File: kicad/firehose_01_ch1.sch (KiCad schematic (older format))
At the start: 82 parts, among them J1 SMA, U1 MAX2112, U2 MAX19505, U20 MIC2090-1YM5, U3 MGA-68563

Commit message: more KiCAD schematic
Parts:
- C31, C32, C33, C34, C35, C36: renamed from C?; value C -> 0.1 uF
- FB11, FB14: value FB -> 240
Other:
- moved on the sheet: C21, C22, C23, C24, C25, C26, C31, C32, C33, C34, C35, C36

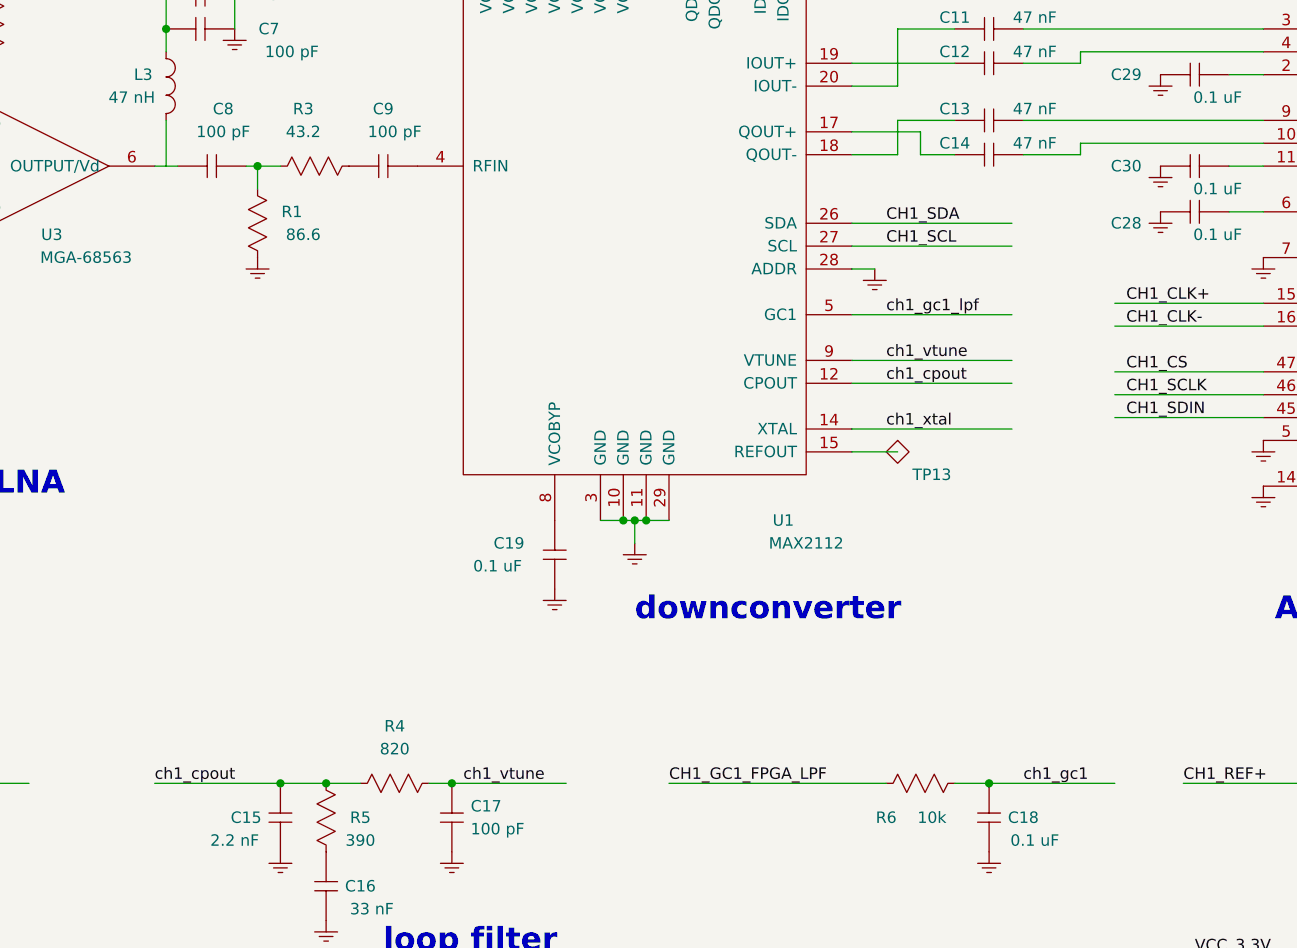
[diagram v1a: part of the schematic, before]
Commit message: fix KiCAD power symbol
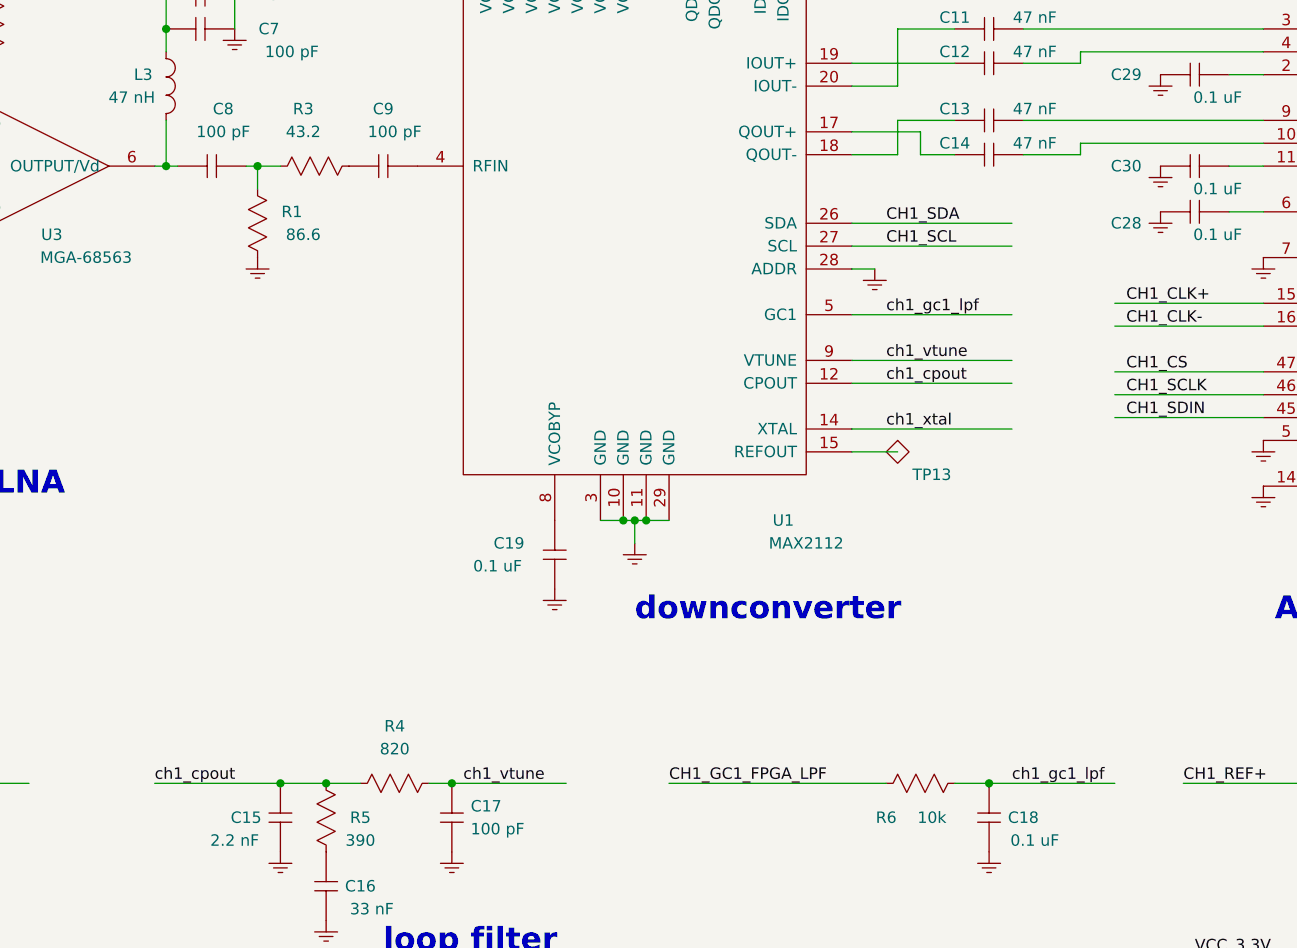
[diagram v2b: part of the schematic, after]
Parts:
- removed PWR? (x25): GND, symbol GND
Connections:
- net labels added: GND
- net labels removed: ch1_gc1
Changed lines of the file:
@@
 EESchema Schematic File Version 2
 LIBS:GNSS_Firehose
-LIBS:device
 LIBS:GNSS_Firehose-cache
 EELAYER 25 0
@@
 $EndComp
 $Comp
-L GND PWR?
+L GND #PWR03
 U 1 1 58CCB8E4
 P 1400 3500
-F 0 "PWR?" H 1600 3400 50  0001 C CNN
+F 0 "#PWR03" H 1600 3400 50  0001 C CNN
 F 1 "GND" H 1600 3300 50  0001 C CNN
 F 2 "" H 1400 3500 50  0001 C CNN
@@
 $EndComp
 $Comp
-L GND PWR?
+L GND #PWR04
 U 1 1 58CCBA24
 P 700 3300
-F 0 "PWR?" H 900 3200 50  0001 C CNN
+F 0 "#PWR04" H 900 3200 50  0001 C CNN
 F 1 "GND" H 900 3100 50  0001 C CNN
 F 2 "" H 700 3300 50  0001 C CNN
@@
 $EndComp
 $Comp
-L GND PWR?
+L GND #PWR05
 U 1 1 58CCC43E
 P 1900 2000
-F 0 "PWR?" H 2100 1900 50  0001 C CNN
+F 0 "#PWR05" H 2100 1900 50  0001 C CNN
 F 1 "GND" H 2100 1800 50  0001 C CNN
 F 2 "" H 1900 2000 50  0001 C CNN
@@
 $EndComp
 $Comp
-L GND PWR?
+L GND #PWR06
 U 1 1 58CCC479
 P 2200 3650
-F 0 "PWR?" H 2400 3550 50  0001 C CNN
+F 0 "#PWR06" H 2400 3550 50  0001 C CNN
 F 1 "GND" H 2400 3450 50  0001 C CNN
 F 2 "" H 2200 3650 50  0001 C CNN
@@
 $EndComp
 $Comp
-L GND PWR?
+L GND #PWR07
 U 1 1 58CCC4B4
 P 3450 3500
-F 0 "PWR?" H 3650 3400 50  0001 C CNN
+F 0 "#PWR07" H 3650 3400 50  0001 C CNN
 F 1 "GND" H 3650 3300 50  0001 C CNN
 F 2 "" H 3450 3500 50  0001 C CNN
@@
 $EndComp
 $Comp
-L GND PWR?
+L GND #PWR08
 U 1 1 58CCC4EF
 P 5100 4750
-F 0 "PWR?" H 5300 4650 50  0001 C CNN
+F 0 "#PWR08" H 5300 4650 50  0001 C CNN
 F 1 "GND" H 5300 4550 50  0001 C CNN
 F 2 "" H 5100 4750 50  0001 C CNN
@@
 $EndComp
 $Comp
-L GND PWR?
+L GND #PWR09
 U 1 1 58CCC5A0
 P 8700 5050
-F 0 "PWR?" H 8900 4950 50  0001 C CNN
+F 0 "#PWR09" H 8900 4950 50  0001 C CNN
 F 1 "GND" H 8900 4850 50  0001 C CNN
 F 2 "" H 8700 5050 50  0001 C CNN
@@
 $EndComp
 $Comp
-L GND PWR?
+L GND #PWR010
 U 1 1 58CCD64A
 P 3350 2500
-F 0 "PWR?" H 3550 2400 50  0001 C CNN
+F 0 "#PWR010" H 3550 2400 50  0001 C CNN
 F 1 "GND" H 3550 2300 50  0001 C CNN
 F 2 "" H 3350 2500 50  0001 C CNN
@@
 $EndComp
 $Comp
-L GND PWR?
+L GND #PWR011
 U 1 1 58CCEBB6
 P 6150 3550
-F 0 "PWR?" H 6350 3450 50  0001 C CNN
+F 0 "#PWR011" H 6350 3450 50  0001 C CNN
 F 1 "GND" H 6350 3350 50  0001 C CNN
 F 2 "" H 6150 3550 50  0001 C CNN
@@
 $EndComp
 $Comp
-L GND PWR?
+L GND #PWR012
 U 1 1 58CCEC6F
 P 4750 4950
-F 0 "PWR?" H 4950 4850 50  0001 C CNN
+F 0 "#PWR012" H 4950 4850 50  0001 C CNN
 F 1 "GND" H 4950 4750 50  0001 C CNN
 F 2 "" H 4750 4950 50  0001 C CNN
@@
 $EndComp
 $Comp
-L GND PWR?
+L GND #PWR013
 U 1 1 58CCF4F3
 P 7400 3300
-F 0 "PWR?" H 7600 3200 50  0001 C CNN
+F 0 "#PWR013" H 7600 3200 50  0001 C CNN
 F 1 "GND" H 7600 3100 50  0001 C CNN
 F 2 "" H 7400 3300 50  0001 C CNN
@@
 $EndComp
 $Comp
-L GND PWR?
+L GND #PWR014
 U 1 1 58CCF5B6
 P 7400 3100
-F 0 "PWR?" H 7600 3000 50  0001 C CNN
+F 0 "#PWR014" H 7600 3000 50  0001 C CNN
 F 1 "GND" H 7600 2900 50  0001 C CNN
 F 2 "" H 7400 3100 50  0001 C CNN
@@
 $EndComp
 $Comp
-L GND PWR?
+L GND #PWR015
 U 1 1 58CCF618
 P 7400 2700
-F 0 "PWR?" H 7600 2600 50  0001 C CNN
+F 0 "#PWR015" H 7600 2600 50  0001 C CNN
 F 1 "GND" H 7600 2500 50  0001 C CNN
 F 2 "" H 7400 2700 50  0001 C CNN
@@
 $EndComp
 $Comp
-L GND PWR?
+L GND #PWR016
 U 1 1 58CD033B
 P 7850 3500
-F 0 "PWR?" H 8050 3400 50  0001 C CNN
+F 0 "#PWR016" H 8050 3400 50  0001 C CNN
 F 1 "GND" H 8050 3300 50  0001 C CNN
 F 2 "" H 7850 3500 50  0001 C CNN
@@
 $EndComp
 $Comp
-L GND PWR?
+L GND #PWR017
 U 1 1 58CD0FE4
 P 7850 4300
-F 0 "PWR?" H 8050 4200 50  0001 C CNN
+F 0 "#PWR017" H 8050 4200 50  0001 C CNN
 F 1 "GND" H 8050 4100 50  0001 C CNN
 F 2 "" H 7850 4300 50  0001 C CNN
@@
 $EndComp
 $Comp
-L GND PWR?
+L GND #PWR018
 U 1 1 58CD1046
 P 7850 4500
-F 0 "PWR?" H 8050 4400 50  0001 C CNN
+F 0 "#PWR018" H 8050 4400 50  0001 C CNN
 F 1 "GND" H 8050 4300 50  0001 C CNN
 F 2 "" H 7850 4500 50  0001 C CNN
@@
 $EndComp
 $Comp
-L GND PWR?
+L GND #PWR019
 U 1 1 58CD3173
 P 2000 6100
-F 0 "PWR?" H 2200 6000 50  0001 C CNN
+F 0 "#PWR019" H 2200 6000 50  0001 C CNN
 F 1 "GND" H 2200 5900 50  0001 C CNN
 F 2 "" H 2000 6100 50  0001 C CNN
@@
 $EndComp
 $Comp
-L GND PWR?
+L GND #PWR020
 U 1 1 58CD31ED
 P 3750 6400
-F 0 "PWR?" H 3950 6300 50  0001 C CNN
+F 0 "#PWR020" H 3950 6300 50  0001 C CNN
 F 1 "GND" H 3950 6200 50  0001 C CNN
 F 2 "" H 3750 6400 50  0001 C CNN
@@
 $EndComp
 $Comp
-L GND PWR?
+L GND #PWR021
 U 1 1 58CD3267
 P 4300 6100
-F 0 "PWR?" H 4500 6000 50  0001 C CNN
+F 0 "#PWR021" H 4500 6000 50  0001 C CNN
 F 1 "GND" H 4500 5900 50  0001 C CNN
 F 2 "" H 4300 6100 50  0001 C CNN
@@
 $EndComp
 $Comp
-L GND PWR?
+L GND #PWR022
 U 1 1 58CD32E1
 P 3550 6100
-F 0 "PWR?" H 3750 6000 50  0001 C CNN
+F 0 "#PWR022" H 3750 6000 50  0001 C CNN
 F 1 "GND" H 3750 5900 50  0001 C CNN
 F 2 "" H 3550 6100 50  0001 C CNN
@@
 ch1_vtune
 $Comp
-L GND PWR?
+L GND #PWR023
 U 1 1 58CD60D0
 P 3450 7350
-F 0 "PWR?" H 3650 7250 50  0001 C CNN
+F 0 "#PWR023" H 3650 7250 50  0001 C CNN
 F 1 "GND" H 3650 7150 50  0001 C CNN
 F 2 "" H 3450 7350 50  0001 C CNN
@@
 $EndComp
 $Comp
-L GND PWR?
+L GND #PWR024
 U 1 1 58CD6BF8
 P 8700 6850
-F 0 "PWR?" H 8900 6750 50  0001 C CNN
+F 0 "#PWR024" H 8900 6750 50  0001 C CNN
 F 1 "GND" H 8900 6650 50  0001 C CNN
 F 2 "" H 8700 6850 50  0001 C CNN
@@
 $EndComp
 $Comp
-L GND PWR?
+L GND #PWR025
 U 1 1 58CD6CAE
 P 9900 6850
-F 0 "PWR?" H 10100 6750 50  0001 C CNN
+F 0 "#PWR025" H 10100 6750 50  0001 C CNN
 F 1 "GND" H 10100 6650 50  0001 C CNN
 F 2 "" H 9900 6850 50  0001 C CNN
@@
 	600  1350 1200 1350
 Wire Wire Line
-	3050 2850 3050 3050
-Wire Wire Line
 	3100 3050 3000 3050
 Wire Wire Line
@@
 Text Label 5250 5750 0    50   ~ 0
 CH1_GC1_FPGA_LPF
-Text Label 6800 5750 0    50   ~ 0
-ch1_gc1
+Text Label 6750 5750 0    50   ~ 0
+ch1_gc1_lpf
 Text Label 7500 5750 0    50   ~ 0
 CH1_REF+
@@
 ch1_xtal
 $Comp
-L GND PWR?
+L GND #PWR026
 U 1 1 58CE2E65
 P 6650 6100
-F 0 "PWR?" H 6850 6000 50  0001 C CNN
+F 0 "#PWR026" H 6850 6000 50  0001 C CNN
 F 1 "GND" H 6850 5900 50  0001 C CNN
 F 2 "" H 6650 6100 50  0001 C CNN
@@
 $EndComp
 $Comp
-L GND PWR?
+L GND #PWR027
 U 1 1 58CE2F1B
 P 8050 6100
-F 0 "PWR?" H 8250 6000 50  0001 C CNN
+F 0 "#PWR027" H 8250 6000 50  0001 C CNN
 F 1 "GND" H 8250 5900 50  0001 C CNN
 F 2 "" H 8050 6100 50  0001 C CNN
@@
 Connection ~ 2200 3600
 Connection ~ 3300 7300
+Wire Wire Line
+	3050 2850 3050 3050
+Connection ~ 3050 3050
 $EndSCHEMATC

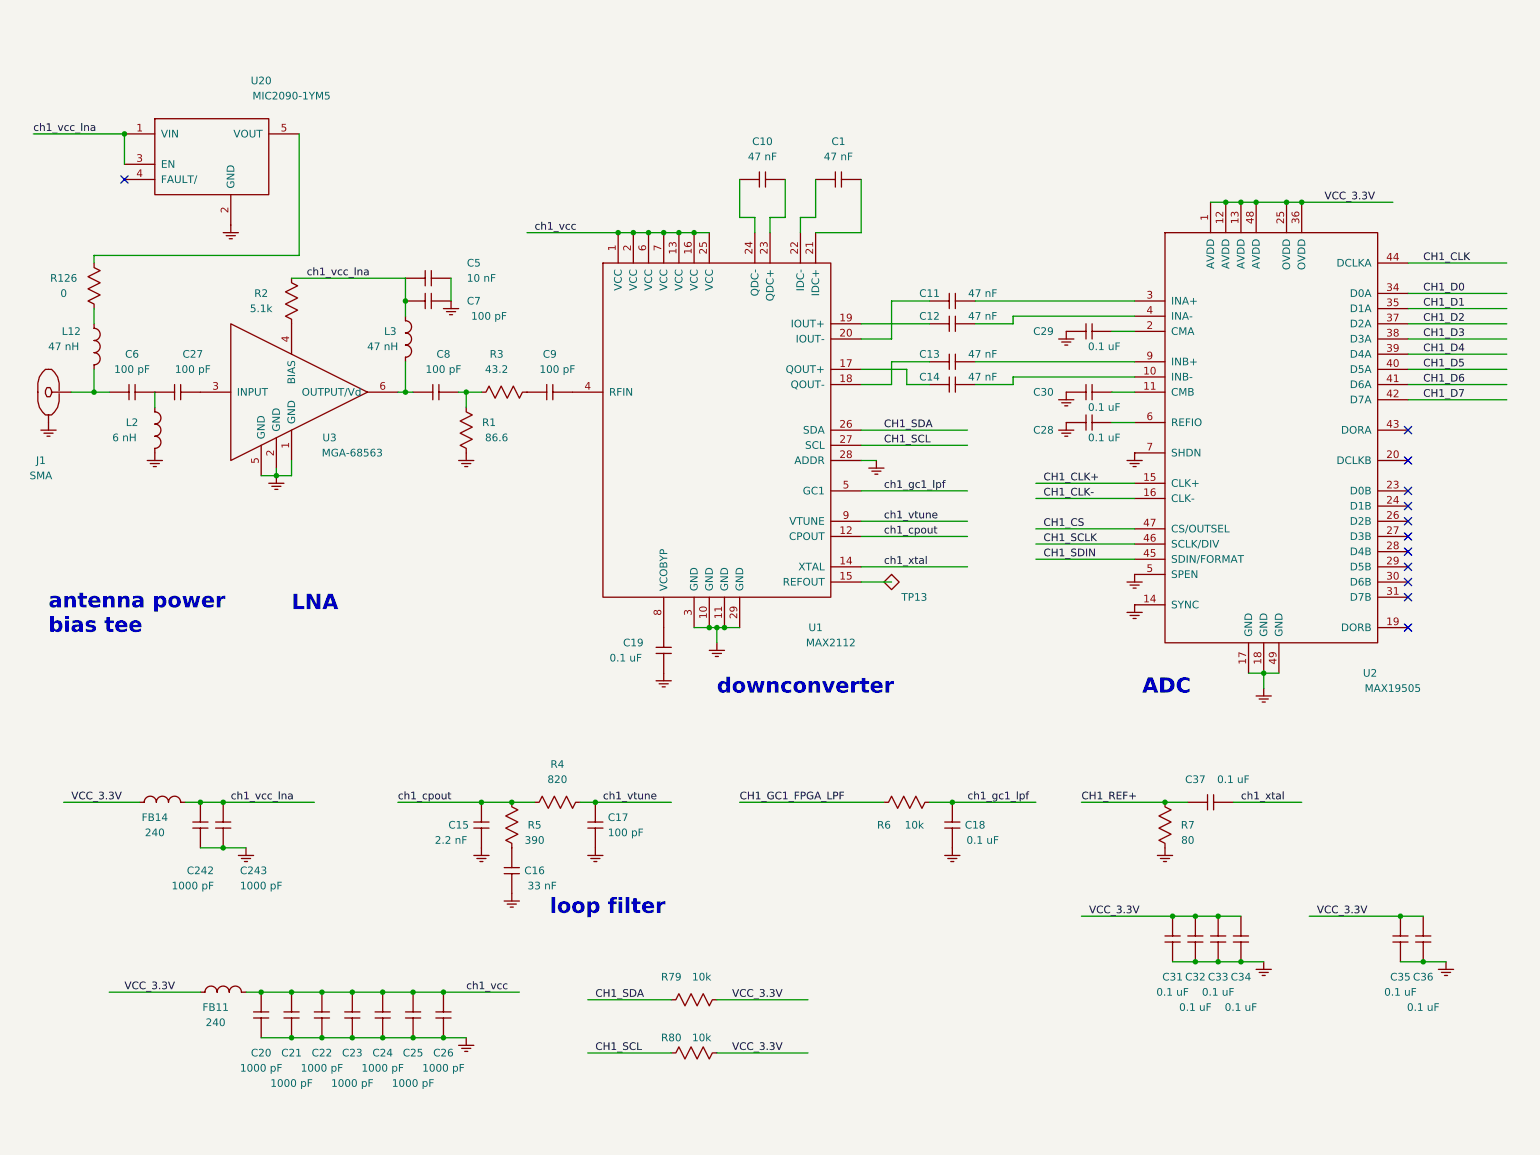
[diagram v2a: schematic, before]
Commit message: schematic, RF channels 2 and 3
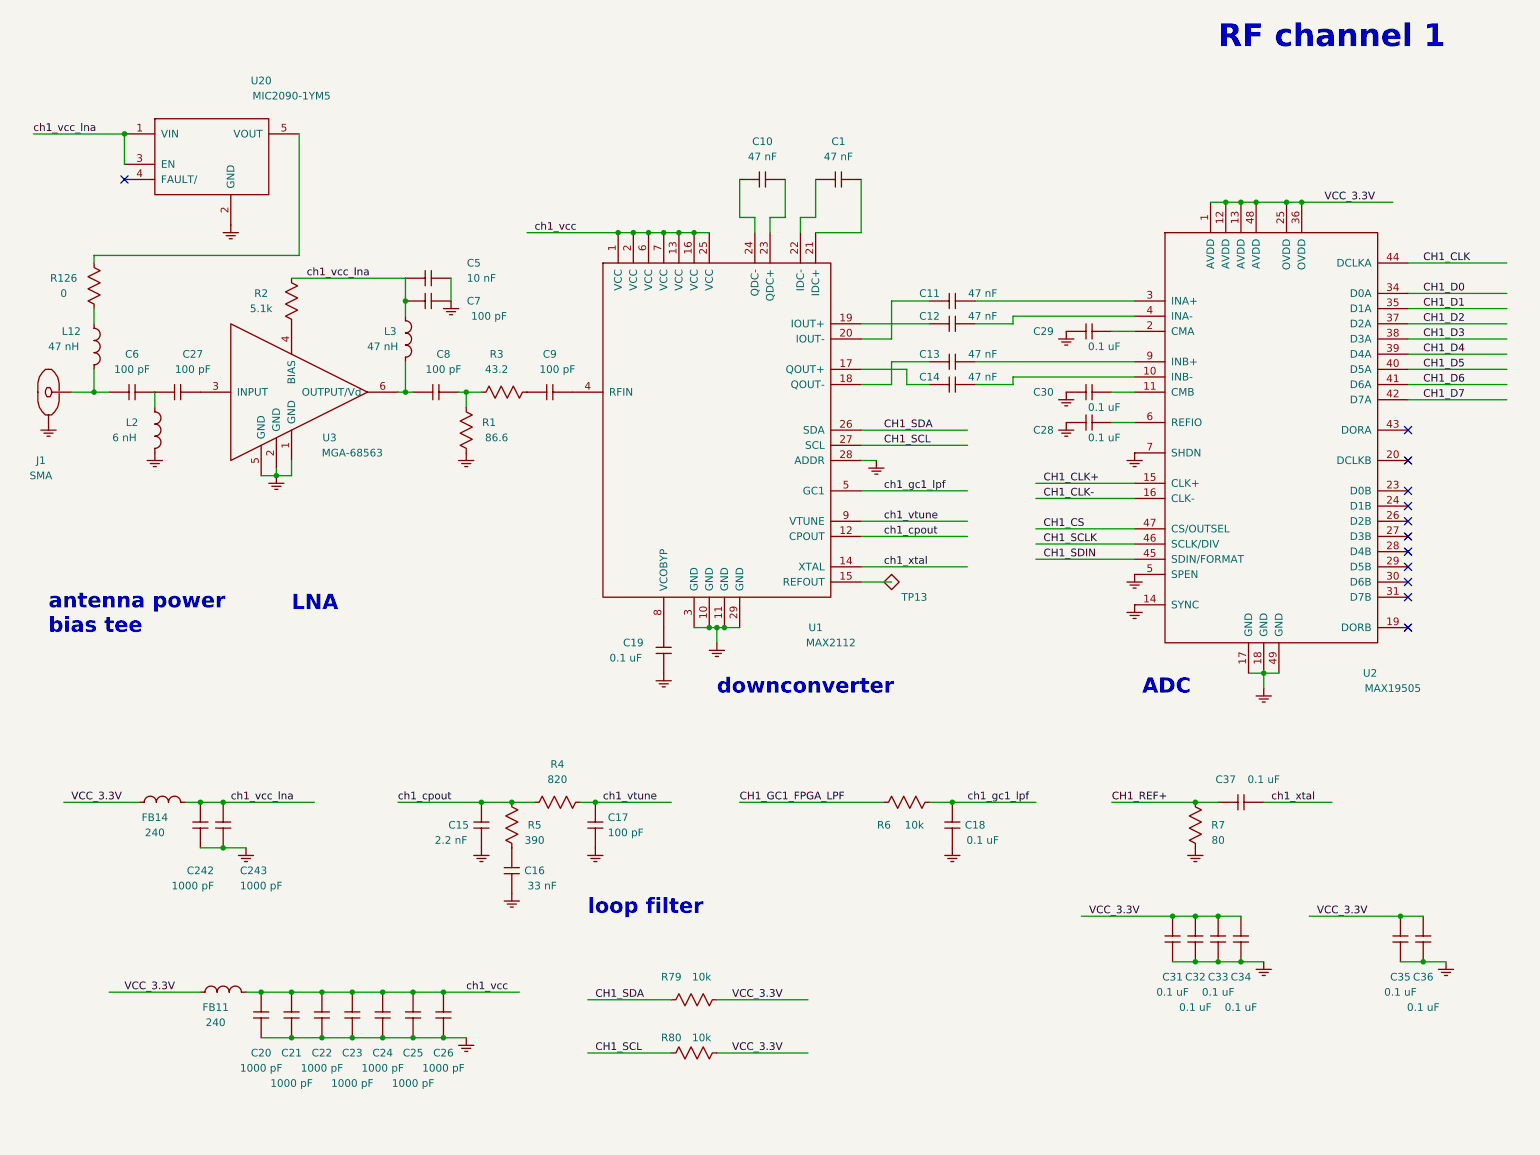
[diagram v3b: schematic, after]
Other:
- note added: "RF channel 1"
- moved on the sheet: C37, R7
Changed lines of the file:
@@
 EESchema Schematic File Version 2
 LIBS:GNSS_Firehose
-LIBS:GNSS_Firehose-cache
 EELAYER 25 0
 EELAYER END
@@
 L R R7
 U 1 1 58CD3547
-P 8050 5900
-F 0 "R7" V 8050 6050 50  0000 C CNN
-F 1 "80" V 8150 6050 50  0000 C CNN
-F 2 "" V 7980 5900 50  0000 C CNN
-F 3 "" H 8050 5900 50  0000 C CNN
-	1    8050 5900
+P 8250 5900
+F 0 "R7" V 8250 6050 50  0000 C CNN
+F 1 "80" V 8350 6050 50  0000 C CNN
+F 2 "" V 8180 5900 50  0000 C CNN
+F 3 "" H 8250 5900 50  0000 C CNN
+	1    8250 5900
 	0    1    1    0
 $EndComp
@@
 L C C37
 U 1 1 58CD362F
-P 8350 5750
-F 0 "C37" H 8250 5900 50  0000 C CNN
-F 1 "0.1 uF" H 8500 5900 50  0000 C CNN
-F 2 "" H 8350 5750 50  0001 C CNN
-F 3 "" H 8350 5750 50  0001 C CNN
-	1    8350 5750
+P 8550 5750
+F 0 "C37" H 8450 5900 50  0000 C CNN
+F 1 "0.1 uF" H 8700 5900 50  0000 C CNN
+F 2 "" H 8550 5750 50  0001 C CNN
+F 3 "" H 8550 5750 50  0001 C CNN
+	1    8550 5750
 	1    0    0    -1
 $EndComp
@@
 Text Notes 7900 5050 0    100  ~ 20
 ADC
-Text Notes 4000 6500 0    100  ~ 20
+Text Notes 4250 6500 0    100  ~ 20
 loop filter
 Text Label 3450 7000 0    50   ~ 0
@@
 VCC_3.3V
 Wire Wire Line
-	7500 5750 8200 5750
-Connection ~ 8050 5750
-Wire Wire Line
-	8500 5750 8950 5750
+	7700 5750 8400 5750
+Connection ~ 8250 5750
+Wire Wire Line
+	8700 5750 9150 5750
 Wire Wire Line
 	6200 5750 5250 5750
@@
 Text Label 6750 5750 0    50   ~ 0
 ch1_gc1_lpf
-Text Label 7500 5750 0    50   ~ 0
+Text Label 7700 5750 0    50   ~ 0
 CH1_REF+
-Text Label 8550 5750 0    50   ~ 0
+Text Label 8750 5750 0    50   ~ 0
 ch1_xtal
 $Comp
@@
 L GND #PWR027
 U 1 1 58CE2F1B
-P 8050 6100
-F 0 "#PWR027" H 8250 6000 50  0001 C CNN
-F 1 "GND" H 8250 5900 50  0001 C CNN
-F 2 "" H 8050 6100 50  0001 C CNN
-F 3 "" H 8050 6100 50  0001 C CNN
-	1    8050 6100
+P 8250 6100
+F 0 "#PWR027" H 8450 6000 50  0001 C CNN
+F 1 "GND" H 8450 5900 50  0001 C CNN
+F 2 "" H 8250 6100 50  0001 C CNN
+F 3 "" H 8250 6100 50  0001 C CNN
+	1    8250 6100
 	1    0    0    -1
 $EndComp
@@
 	3050 2850 3050 3050
 Connection ~ 3050 3050
+Text Notes 8400 800  0    150  ~ 30
+RF channel 1
 $EndSCHEMATC
